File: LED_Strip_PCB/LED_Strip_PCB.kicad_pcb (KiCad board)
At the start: 2 copper layers, 12 parts

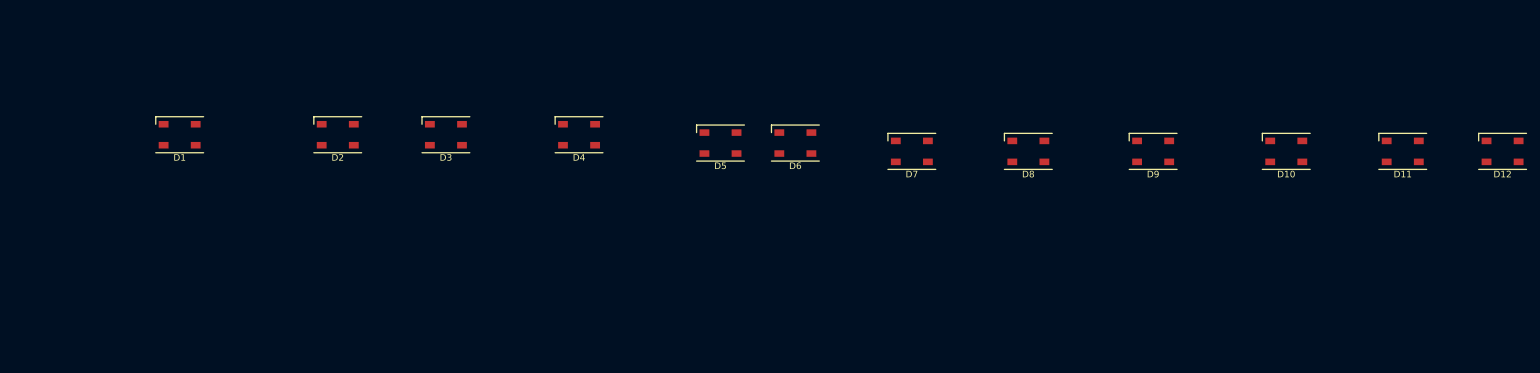
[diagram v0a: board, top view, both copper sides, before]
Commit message: PCB now has 3 LED strips and perforation
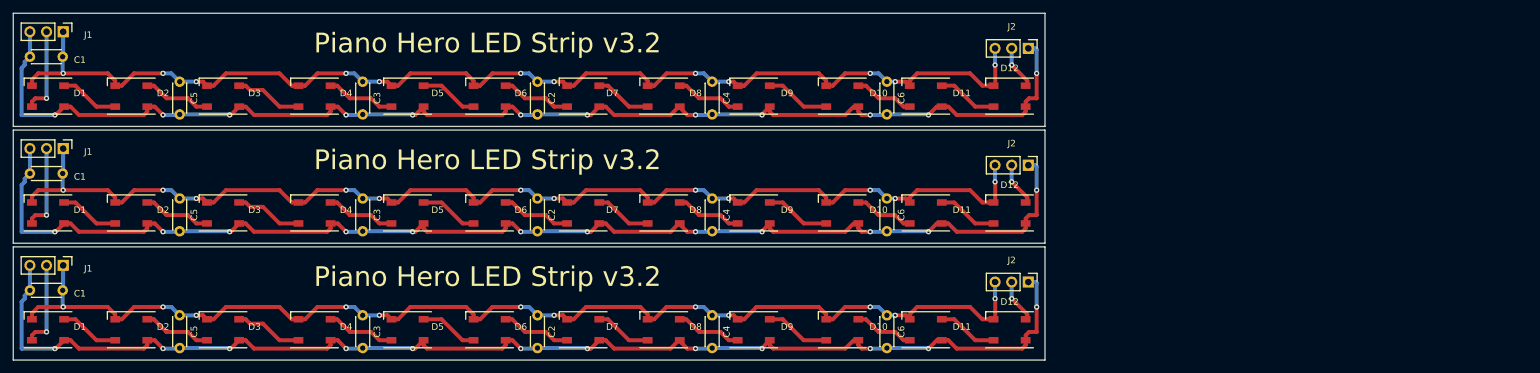
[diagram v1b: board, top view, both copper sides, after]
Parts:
- added C1: C_Small, Capacitor_THT:C_Disc_D4.3mm_W1.9mm_P5.00mm, F.Cu at (25.4, 88.5)
- added C1: C_Small, Capacitor_THT:C_Disc_D4.3mm_W1.9mm_P5.00mm, F.Cu at (25.4, 70.7)
- added C1: C_Small, Capacitor_THT:C_Disc_D4.3mm_W1.9mm_P5.00mm, F.Cu at (25.4, 52.9)
- added C2: C_Small, Capacitor_THT:C_Disc_D4.3mm_W1.9mm_P5.00mm, F.Cu at (102.9, 92.3)
- added C2: C_Small, Capacitor_THT:C_Disc_D4.3mm_W1.9mm_P5.00mm, F.Cu at (102.9, 74.5)
- added C2: C_Small, Capacitor_THT:C_Disc_D4.3mm_W1.9mm_P5.00mm, F.Cu at (102.9, 56.7)
- added C3: C_Small, Capacitor_THT:C_Disc_D4.3mm_W1.9mm_P5.00mm, F.Cu at (76.2, 92.3)
- added C3: C_Small, Capacitor_THT:C_Disc_D4.3mm_W1.9mm_P5.00mm, F.Cu at (76.2, 74.5)
- added C3: C_Small, Capacitor_THT:C_Disc_D4.3mm_W1.9mm_P5.00mm, F.Cu at (76.2, 56.7)
- added C4: C_Small, Capacitor_THT:C_Disc_D4.3mm_W1.9mm_P5.00mm, F.Cu at (129.5, 92.3)
- added C4: C_Small, Capacitor_THT:C_Disc_D4.3mm_W1.9mm_P5.00mm, F.Cu at (129.5, 74.5)
- added C4: C_Small, Capacitor_THT:C_Disc_D4.3mm_W1.9mm_P5.00mm, F.Cu at (129.5, 56.7)
- added C5: C_Small, Capacitor_THT:C_Disc_D4.3mm_W1.9mm_P5.00mm, F.Cu at (48.3, 92.3)
- added C5: C_Small, Capacitor_THT:C_Disc_D4.3mm_W1.9mm_P5.00mm, F.Cu at (48.3, 74.5)
- added C5: C_Small, Capacitor_THT:C_Disc_D4.3mm_W1.9mm_P5.00mm, F.Cu at (48.3, 56.7)
- added C6: C_Small, Capacitor_THT:C_Disc_D4.3mm_W1.9mm_P5.00mm, F.Cu at (156.2, 92.3)
- added C6: C_Small, Capacitor_THT:C_Disc_D4.3mm_W1.9mm_P5.00mm, F.Cu at (156.2, 74.5)
- added C6: C_Small, Capacitor_THT:C_Disc_D4.3mm_W1.9mm_P5.00mm, F.Cu at (156.2, 56.7)
- added D1: SK6812, LED_SMD:LED_SK6812_PLCC4_5.0x5.0mm_P3.2mm, F.Cu at (28.2, 94.5)
- added D1: SK6812, LED_SMD:LED_SK6812_PLCC4_5.0x5.0mm_P3.2mm, F.Cu at (28.2, 76.7)
- added D10: SK6812, LED_SMD:LED_SK6812_PLCC4_5.0x5.0mm_P3.2mm, F.Cu at (149.4, 94.5)
- added D10: SK6812, LED_SMD:LED_SK6812_PLCC4_5.0x5.0mm_P3.2mm, F.Cu at (149.4, 76.7)
- added D11: SK6812, LED_SMD:LED_SK6812_PLCC4_5.0x5.0mm_P3.2mm, F.Cu at (162.1, 94.5)
- added D11: SK6812, LED_SMD:LED_SK6812_PLCC4_5.0x5.0mm_P3.2mm, F.Cu at (162.1, 76.7)
- added D12: SK6812, LED_SMD:LED_SK6812_PLCC4_5.0x5.0mm_P3.2mm, F.Cu at (174.9, 94.5)
- added D12: SK6812, LED_SMD:LED_SK6812_PLCC4_5.0x5.0mm_P3.2mm, F.Cu at (174.9, 76.7)
- added D2: SK6812, LED_SMD:LED_SK6812_PLCC4_5.0x5.0mm_P3.2mm, F.Cu at (40.9, 94.5)
- added D2: SK6812, LED_SMD:LED_SK6812_PLCC4_5.0x5.0mm_P3.2mm, F.Cu at (40.9, 76.7)
- added D3: SK6812, LED_SMD:LED_SK6812_PLCC4_5.0x5.0mm_P3.2mm, F.Cu at (54.9, 94.5)
- added D3: SK6812, LED_SMD:LED_SK6812_PLCC4_5.0x5.0mm_P3.2mm, F.Cu at (54.9, 76.7)
- added D4: SK6812, LED_SMD:LED_SK6812_PLCC4_5.0x5.0mm_P3.2mm, F.Cu at (68.8, 94.5)
- added D4: SK6812, LED_SMD:LED_SK6812_PLCC4_5.0x5.0mm_P3.2mm, F.Cu at (68.8, 76.7)
- added D5: SK6812, LED_SMD:LED_SK6812_PLCC4_5.0x5.0mm_P3.2mm, F.Cu at (83.0, 94.5)
- added D5: SK6812, LED_SMD:LED_SK6812_PLCC4_5.0x5.0mm_P3.2mm, F.Cu at (83.0, 76.7)
- added D6: SK6812, LED_SMD:LED_SK6812_PLCC4_5.0x5.0mm_P3.2mm, F.Cu at (95.6, 94.5)
- added D6: SK6812, LED_SMD:LED_SK6812_PLCC4_5.0x5.0mm_P3.2mm, F.Cu at (95.6, 76.7)
- added D7: SK6812, LED_SMD:LED_SK6812_PLCC4_5.0x5.0mm_P3.2mm, F.Cu at (109.8, 94.5)
- added D7: SK6812, LED_SMD:LED_SK6812_PLCC4_5.0x5.0mm_P3.2mm, F.Cu at (109.8, 76.7)
- added D8: SK6812, LED_SMD:LED_SK6812_PLCC4_5.0x5.0mm_P3.2mm, F.Cu at (122.1, 94.5)
- added D8: SK6812, LED_SMD:LED_SK6812_PLCC4_5.0x5.0mm_P3.2mm, F.Cu at (122.1, 76.7)
- added D9: SK6812, LED_SMD:LED_SK6812_PLCC4_5.0x5.0mm_P3.2mm, F.Cu at (135.9, 94.5)
- added D9: SK6812, LED_SMD:LED_SK6812_PLCC4_5.0x5.0mm_P3.2mm, F.Cu at (135.9, 76.7)
- added J1: Conn_01x03_Female, Connector_PinHeader_2.54mm:PinHeader_1x03_P2.54mm_Vertical, F.Cu at (30.5, 84.7)
- added J1: Conn_01x03_Female, Connector_PinHeader_2.54mm:PinHeader_1x03_P2.54mm_Vertical, F.Cu at (30.5, 66.9)
- added J1: Conn_01x03_Female, Connector_PinHeader_2.54mm:PinHeader_1x03_P2.54mm_Vertical, F.Cu at (30.5, 49.0)
- added J2: Conn_01x03_Female, Connector_PinHeader_2.54mm:PinHeader_1x03_P2.54mm_Vertical, F.Cu at (177.8, 87.2)
- added J2: Conn_01x03_Female, Connector_PinHeader_2.54mm:PinHeader_1x03_P2.54mm_Vertical, F.Cu at (177.8, 69.4)
- added J2: Conn_01x03_Female, Connector_PinHeader_2.54mm:PinHeader_1x03_P2.54mm_Vertical, F.Cu at (177.8, 51.6)
- added REF**: MountingHole_0.52mm, MountingHole:MountingHole_0.52mm, F.Cu at (36.9, 81.6)
- added REF**: MountingHole_0.52mm, MountingHole:MountingHole_0.52mm, F.Cu at (84.9, 63.8)
- added REF**: MountingHole_0.52mm, MountingHole:MountingHole_0.52mm, F.Cu at (60.9, 63.8)
- added REF**: MountingHole_0.52mm, MountingHole:MountingHole_0.52mm, F.Cu at (36.9, 63.8)
- added REF**: MountingHole_0.52mm, MountingHole:MountingHole_0.52mm, F.Cu at (84.9, 81.6)
- added REF**: MountingHole_0.52mm, MountingHole:MountingHole_0.52mm, F.Cu at (60.9, 81.6)
- added REF**: MountingHole_0.52mm, MountingHole:MountingHole_0.52mm, F.Cu at (161.7, 81.6)
- added REF**: MountingHole_0.52mm, MountingHole:MountingHole_0.52mm, F.Cu at (132.9, 81.6)
- added REF**: MountingHole_0.52mm, MountingHole:MountingHole_0.52mm, F.Cu at (108.9, 81.6)
- added REF**: MountingHole_0.52mm, MountingHole:MountingHole_0.52mm, F.Cu at (161.7, 63.8)
- added REF**: MountingHole_0.52mm, MountingHole:MountingHole_0.52mm, F.Cu at (132.9, 63.8)
- added REF**: MountingHole_0.52mm, MountingHole:MountingHole_0.52mm, F.Cu at (108.9, 63.8)
- moved D12 75.7 mm to (174.9, 58.9)
- moved D11 73.3 mm to (162.1, 58.9)
- moved D10 68.3 mm to (149.4, 58.9)
- moved D9 61.5 mm to (135.9, 58.9)
- moved D8 56.3 mm to (122.1, 58.9)
- moved D7 50.9 mm to (109.8, 58.9)
- moved D5 48.3 mm to (83.0, 58.9)
- moved D6 47.2 mm to (95.6, 58.9)
- moved D4 40.8 mm to (68.8, 58.9)
- moved D3 34.5 mm to (54.9, 58.9)
- moved D2 32.1 mm to (40.9, 58.9)
- moved D1 20.9 mm to (28.2, 58.9)
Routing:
- net Net-(C1-Pad1): track 0.00 -> 578.6 mm, vias 0 -> 36
- net Net-(C1-Pad2): track 0.00 -> 539.3 mm, vias 0 -> 36
- net Net-(D1-Pad2): track 0.00 -> 40.1 mm, vias 0 -> 3
- net Net-(D6-Pad4): track 0.00 -> 32.1 mm
- net Net-(D4-Pad4): track 0.00 -> 31.9 mm
- net Net-(D2-Pad4): track 0.00 -> 31.3 mm
- net Net-(D3-Pad4): track 0.00 -> 31.2 mm
- net Net-(D8-Pad4): track 0.00 -> 30.5 mm
- net Net-(D10-Pad2): track 0.00 -> 29.8 mm
- net Net-(D11-Pad4): track 0.00 -> 27.7 mm
- net Net-(D10-Pad4): track 0.00 -> 27.5 mm
- net Net-(D1-Pad4): track 0.00 -> 27.4 mm
- net Net-(D5-Pad4): track 0.00 -> 26.9 mm
- net Net-(D7-Pad4): track 0.00 -> 26.2 mm
- net Net-(D12-Pad4): track 0.00 -> 20.0 mm, vias 0 -> 3
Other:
- board outline added: 157.5 x 52.9 mm
- net class Default: trace_width 0.25 -> 0.6
- rule trace_min: 0.2 -> 0.6
- board text added: "Piano Hero LED Strip v3.2"
